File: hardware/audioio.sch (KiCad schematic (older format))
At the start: 7 parts

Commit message: Start placement of parts
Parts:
- C22, C23: footprint (none) -> footprints:SMD0805-CAP-M
- D7, D8: footprint (none) -> footprints:SOT23-M
- FB3, FB4, FB5: footprint (none) -> footprints:SMD0805-FERRITE-M
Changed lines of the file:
@@
 $Descr A4 11693 8268
 encoding utf-8
-Sheet 6 6
+Sheet 4 6
 Title "poppimASiina Audio IO protection"
 Date "2016-05-21"
@@
 AR Path="/5741BEDA/573ECF35" Ref="FB6"  Part="1"
 AR Path="/5741C4B9/573ECF35" Ref="FB9"  Part="1"
-F 0 "FB9" H 6950 3550 50  0000 C CNN
+F 0 "FB3" H 6950 3550 50  0000 C CNN
 F 1 "FILTER" H 7000 3450 50  0000 C CNN
-F 2 "" H 7100 3300 50  0000 C CNN
+F 2 "footprints:SMD0805-FERRITE-M" H 7100 3300 50  0001 C CNN
 F 3 "" H 7100 3300 50  0000 C CNN
 	1    7100 3300
@@
 AR Path="/5741BEDA/573EEC33" Ref="FB7"  Part="1"
 AR Path="/5741C4B9/573EEC33" Ref="FB10"  Part="1"
-F 0 "FB10" H 6950 3300 50  0000 C CNN
+F 0 "FB4" H 6950 3300 50  0000 C CNN
 F 1 "FILTER" H 7000 3400 50  0000 C CNN
-F 2 "" H 7100 3500 50  0000 C CNN
+F 2 "footprints:SMD0805-FERRITE-M" H 7100 3500 50  0001 C CNN
 F 3 "" H 7100 3500 50  0000 C CNN
 	1    7100 3500
@@
 AR Path="/5741BEDA/573F1279" Ref="C24"  Part="1"
 AR Path="/5741C4B9/573F1279" Ref="C26"  Part="1"
-F 0 "C26" H 6225 4000 50  0000 L CNN
+F 0 "C22" H 6225 4000 50  0000 L CNN
 F 1 "47p" H 6225 3800 50  0000 L CNN
-F 2 "" H 6238 3750 50  0000 C CNN
+F 2 "footprints:SMD0805-CAP-M" H 6238 3750 50  0001 C CNN
 F 3 "" H 6200 3900 50  0000 C CNN
 	1    6200 3900
@@
 AR Path="/5741BEDA/573F1460" Ref="C25"  Part="1"
 AR Path="/5741C4B9/573F1460" Ref="C27"  Part="1"
-F 0 "C27" H 6475 4000 50  0000 L CNN
+F 0 "C23" H 6475 4000 50  0000 L CNN
 F 1 "47p" H 6475 3800 50  0000 L CNN
-F 2 "" H 6488 3750 50  0000 C CNN
+F 2 "footprints:SMD0805-CAP-M" H 6488 3750 50  0001 C CNN
 F 3 "" H 6450 3900 50  0000 C CNN
 	1    6450 3900
@@
 $EndComp
 $Comp
-L GNDA #PWR45
+L GNDA #PWR045
 U 1 1 573F1A89
 P 6450 4200
-AR Path="/574185DC/573F1A89" Ref="#PWR45"  Part="1"
-AR Path="/5741BEDA/573F1A89" Ref="#PWR46"  Part="1"
-AR Path="/5741C4B9/573F1A89" Ref="#PWR47"  Part="1"
-F 0 "#PWR47" H 6450 3950 50  0001 C CNN
+AR Path="/574185DC/573F1A89" Ref="#PWR045"  Part="1"
+AR Path="/5741BEDA/573F1A89" Ref="#PWR046"  Part="1"
+AR Path="/5741C4B9/573F1A89" Ref="#PWR047"  Part="1"
+F 0 "#PWR045" H 6450 3950 50  0001 C CNN
 F 1 "GNDA" H 6450 4050 50  0000 C CNN
 F 2 "" H 6450 4200 50  0000 C CNN
@@
 AR Path="/5741BEDA/573F8794" Ref="D9"  Part="1"
 AR Path="/5741C4B9/573F8794" Ref="D11"  Part="1"
-F 0 "D11" H 5300 3150 50  0000 C CNN
+F 0 "D7" H 5300 3150 50  0000 C CNN
 F 1 "BAT54S" H 5300 3050 50  0000 C CNN
-F 2 "" H 5300 2950 50  0000 C CNN
+F 2 "footprints:SOT23-M" H 5300 2950 50  0001 C CNN
 F 3 "" H 5300 2950 50  0000 C CNN
 	1    5300 2950
@@
 AR Path="/5741BEDA/573F8863" Ref="D10"  Part="1"
 AR Path="/5741C4B9/573F8863" Ref="D12"  Part="1"
-F 0 "D12" H 5300 3950 50  0000 C CNN
+F 0 "D8" H 5300 3950 50  0000 C CNN
 F 1 "BAT54S" H 5300 3850 50  0000 C CNN
-F 2 "" H 5300 3750 50  0000 C CNN
+F 2 "footprints:SOT23-M" H 5300 3750 50  0001 C CNN
 F 3 "" H 5300 3750 50  0000 C CNN
 	1    5300 3750
@@
 AR Path="/5741BEDA/5741A7F2" Ref="FB8"  Part="1"
 AR Path="/5741C4B9/5741A7F2" Ref="FB11"  Part="1"
-F 0 "FB11" H 6950 4400 50  0000 C CNN
+F 0 "FB5" H 6950 4400 50  0000 C CNN
 F 1 "FILTER" H 7000 4300 50  0000 C CNN
-F 2 "" H 7100 4150 50  0000 C CNN
+F 2 "footprints:SMD0805-FERRITE-M" H 7100 4150 50  0001 C CNN
 F 3 "" H 7100 4150 50  0000 C CNN
 	1    7100 4150

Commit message: Add resistors from audio IO to gnd, fixes #10
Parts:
- added R? (x2): 1Meg5, symbol R
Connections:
- net GNDA: now also R?.2, R?.2
- net LEFT_DEVICE: now also R?.1
- net RIGHT_DEVICE: now also R?.1
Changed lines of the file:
@@
 $Descr A4 11693 8268
 encoding utf-8
-Sheet 4 6
+Sheet 6 6
 Title "poppimASiina Audio IO protection"
 Date "2016-05-21"
@@
 RF filtering
 Wire Wire Line
-	4350 3500 6750 3500
-Wire Wire Line
-	4350 3300 6750 3300
+	3200 3500 6750 3500
+Wire Wire Line
+	3200 3300 6750 3300
 Wire Wire Line
 	5300 3300 5300 3150
@@
 AR Path="/5741BEDA/573ECF35" Ref="FB6"  Part="1"
 AR Path="/5741C4B9/573ECF35" Ref="FB9"  Part="1"
-F 0 "FB3" H 6950 3550 50  0000 C CNN
+F 0 "FB9" H 6950 3550 50  0000 C CNN
 F 1 "FILTER" H 7000 3450 50  0000 C CNN
 F 2 "footprints:SMD0805-FERRITE-M" H 7100 3300 50  0001 C CNN
@@
 AR Path="/5741BEDA/573EEC33" Ref="FB7"  Part="1"
 AR Path="/5741C4B9/573EEC33" Ref="FB10"  Part="1"
-F 0 "FB4" H 6950 3300 50  0000 C CNN
+F 0 "FB10" H 6950 3300 50  0000 C CNN
 F 1 "FILTER" H 7000 3400 50  0000 C CNN
 F 2 "footprints:SMD0805-FERRITE-M" H 7100 3500 50  0001 C CNN
@@
 AR Path="/5741BEDA/573F1279" Ref="C24"  Part="1"
 AR Path="/5741C4B9/573F1279" Ref="C26"  Part="1"
-F 0 "C22" H 6225 4000 50  0000 L CNN
+F 0 "C26" H 6225 4000 50  0000 L CNN
 F 1 "47p" H 6225 3800 50  0000 L CNN
 F 2 "footprints:SMD0805-CAP-M" H 6238 3750 50  0001 C CNN
@@
 AR Path="/5741BEDA/573F1460" Ref="C25"  Part="1"
 AR Path="/5741C4B9/573F1460" Ref="C27"  Part="1"
-F 0 "C23" H 6475 4000 50  0000 L CNN
+F 0 "C27" H 6475 4000 50  0000 L CNN
 F 1 "47p" H 6475 3800 50  0000 L CNN
 F 2 "footprints:SMD0805-CAP-M" H 6488 3750 50  0001 C CNN
@@
 AR Path="/5741BEDA/573F1A89" Ref="#PWR046"  Part="1"
 AR Path="/5741C4B9/573F1A89" Ref="#PWR047"  Part="1"
-F 0 "#PWR045" H 6450 3950 50  0001 C CNN
+F 0 "#PWR047" H 6450 3950 50  0001 C CNN
 F 1 "GNDA" H 6450 4050 50  0000 C CNN
 F 2 "" H 6450 4200 50  0000 C CNN
@@
 AR Path="/5741BEDA/573F8794" Ref="D9"  Part="1"
 AR Path="/5741C4B9/573F8794" Ref="D11"  Part="1"
-F 0 "D7" H 5300 3150 50  0000 C CNN
+F 0 "D11" H 5300 3150 50  0000 C CNN
 F 1 "BAT54S" H 5300 3050 50  0000 C CNN
 F 2 "footprints:SOT23-M" H 5300 2950 50  0001 C CNN
@@
 AR Path="/5741BEDA/573F8863" Ref="D10"  Part="1"
 AR Path="/5741C4B9/573F8863" Ref="D12"  Part="1"
-F 0 "D8" H 5300 3950 50  0000 C CNN
+F 0 "D12" H 5300 3950 50  0000 C CNN
 F 1 "BAT54S" H 5300 3850 50  0000 C CNN
 F 2 "footprints:SOT23-M" H 5300 3750 50  0001 C CNN
@@
 Text HLabel 7800 3400 2    60   BiDi ~ 0
 GROUND_CABLE
-Text HLabel 4350 3300 0    60   BiDi ~ 0
+Text HLabel 3200 3300 0    60   BiDi ~ 0
 LEFT_DEVICE
-Text HLabel 4350 3500 0    60   BiDi ~ 0
+Text HLabel 3200 3500 0    60   BiDi ~ 0
 RIGHT_DEVICE
 Text HLabel 4900 3750 0    60   Input ~ 0
@@
 AR Path="/5741BEDA/5741A7F2" Ref="FB8"  Part="1"
 AR Path="/5741C4B9/5741A7F2" Ref="FB11"  Part="1"
-F 0 "FB5" H 6950 4400 50  0000 C CNN
+F 0 "FB11" H 6950 4400 50  0000 C CNN
 F 1 "FILTER" H 7000 4300 50  0000 C CNN
 F 2 "footprints:SMD0805-FERRITE-M" H 7100 4150 50  0001 C CNN
@@
 Wire Wire Line
 	6200 4050 6200 4150
+$Comp
+L R R?
+U 1 1 57493FA0
+P 3500 3750
+F 0 "R?" V 3580 3750 50  0000 C CNN
+F 1 "1Meg5" V 3400 3750 50  0000 C CNN
+F 2 "" V 3430 3750 50  0000 C CNN
+F 3 "" H 3500 3750 50  0000 C CNN
+	1    3500 3750
+	1    0    0    -1
+$EndComp
+$Comp
+L R R?
+U 1 1 57493FED
+P 3750 3750
+F 0 "R?" V 3830 3750 50  0000 C CNN
+F 1 "1Meg5" V 3650 3750 50  0000 C CNN
+F 2 "" V 3680 3750 50  0000 C CNN
+F 3 "" H 3750 3750 50  0000 C CNN
+	1    3750 3750
+	1    0    0    -1
+$EndComp
+Wire Wire Line
+	3750 3600 3750 3300
+Connection ~ 3750 3300
+Wire Wire Line
+	3500 3600 3500 3500
+Connection ~ 3500 3500
+$Comp
+L GNDA #PWR?
+U 1 1 57494606
+P 3750 4150
+F 0 "#PWR?" H 3750 3900 50  0001 C CNN
+F 1 "GNDA" H 3750 4000 50  0000 C CNN
+F 2 "" H 3750 4150 50  0000 C CNN
+F 3 "" H 3750 4150 50  0000 C CNN
+	1    3750 4150
+	1    0    0    -1
+$EndComp
+Wire Wire Line
+	3750 3900 3750 4150
+Wire Wire Line
+	3500 3900 3500 4000
+Wire Wire Line
+	3500 4000 3750 4000
+Connection ~ 3750 4000
 $EndSCHEMATC

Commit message: Fix #8
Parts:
- gave numbers to parts that had none: 2
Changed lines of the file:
@@
 $EndComp
 $Comp
-L GNDA #PWR045
+L GNDA #PWR047
 U 1 1 573F1A89
 P 6450 4200
-AR Path="/574185DC/573F1A89" Ref="#PWR045"  Part="1"
-AR Path="/5741BEDA/573F1A89" Ref="#PWR046"  Part="1"
-AR Path="/5741C4B9/573F1A89" Ref="#PWR047"  Part="1"
-F 0 "#PWR047" H 6450 3950 50  0001 C CNN
+AR Path="/574185DC/573F1A89" Ref="#PWR047"  Part="1"
+AR Path="/5741BEDA/573F1A89" Ref="#PWR049"  Part="1"
+AR Path="/5741C4B9/573F1A89" Ref="#PWR051"  Part="1"
+F 0 "#PWR051" H 6450 3950 50  0001 C CNN
 F 1 "GNDA" H 6450 4050 50  0000 C CNN
 F 2 "" H 6450 4200 50  0000 C CNN
@@
 	6200 4050 6200 4150
 $Comp
-L R R?
+L R R601
 U 1 1 57493FA0
 P 3500 3750
-F 0 "R?" V 3580 3750 50  0000 C CNN
+AR Path="/5741C4B9/57493FA0" Ref="R601"  Part="1"
+AR Path="/574185DC/57493FA0" Ref="R401"  Part="1"
+AR Path="/5741BEDA/57493FA0" Ref="R501"  Part="1"
+F 0 "R601" V 3580 3750 50  0000 C CNN
 F 1 "1Meg5" V 3400 3750 50  0000 C CNN
 F 2 "" V 3430 3750 50  0000 C CNN
@@
 $EndComp
 $Comp
-L R R?
+L R R602
 U 1 1 57493FED
 P 3750 3750
-F 0 "R?" V 3830 3750 50  0000 C CNN
+AR Path="/5741C4B9/57493FED" Ref="R602"  Part="1"
+AR Path="/574185DC/57493FED" Ref="R402"  Part="1"
+AR Path="/5741BEDA/57493FED" Ref="R502"  Part="1"
+F 0 "R602" V 3830 3750 50  0000 C CNN
 F 1 "1Meg5" V 3650 3750 50  0000 C CNN
 F 2 "" V 3680 3750 50  0000 C CNN
@@
 Connection ~ 3500 3500
 $Comp
-L GNDA #PWR?
+L GNDA #PWR052
 U 1 1 57494606
 P 3750 4150
-F 0 "#PWR?" H 3750 3900 50  0001 C CNN
+AR Path="/5741C4B9/57494606" Ref="#PWR052"  Part="1"
+AR Path="/574185DC/57494606" Ref="#PWR048"  Part="1"
+AR Path="/5741BEDA/57494606" Ref="#PWR050"  Part="1"
+F 0 "#PWR052" H 3750 3900 50  0001 C CNN
 F 1 "GNDA" H 3750 4000 50  0000 C CNN
 F 2 "" H 3750 4150 50  0000 C CNN

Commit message: Update schematics
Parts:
- R29: renamed from R601; footprint (none) -> footprints:SMD0805-RES-M
- R30: renamed from R602; footprint (none) -> footprints:SMD0805-RES-M
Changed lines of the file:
@@
 $EndComp
 $Comp
-L GNDA #PWR048
+L GNDA #PWR51
 U 1 1 573F1A89
 P 6450 4200
-AR Path="/574185DC/573F1A89" Ref="#PWR048"  Part="1"
-AR Path="/5741BEDA/573F1A89" Ref="#PWR050"  Part="1"
-AR Path="/5741C4B9/573F1A89" Ref="#PWR052"  Part="1"
-F 0 "#PWR052" H 6450 3950 50  0001 C CNN
+AR Path="/574185DC/573F1A89" Ref="#PWR51"  Part="1"
+AR Path="/5741BEDA/573F1A89" Ref="#PWR53"  Part="1"
+AR Path="/5741C4B9/573F1A89" Ref="#PWR55"  Part="1"
+F 0 "#PWR55" H 6450 3950 50  0001 C CNN
 F 1 "GNDA" H 6450 4050 50  0000 C CNN
 F 2 "" H 6450 4200 50  0000 C CNN
@@
 	6200 4050 6200 4150
 $Comp
-L R R601
+L R R29
 U 1 1 57493FA0
 P 3500 3750
-AR Path="/5741C4B9/57493FA0" Ref="R601"  Part="1"
-AR Path="/574185DC/57493FA0" Ref="R401"  Part="1"
-AR Path="/5741BEDA/57493FA0" Ref="R501"  Part="1"
-F 0 "R601" V 3580 3750 50  0000 C CNN
+AR Path="/5741C4B9/57493FA0" Ref="R29"  Part="1"
+AR Path="/574185DC/57493FA0" Ref="R25"  Part="1"
+AR Path="/5741BEDA/57493FA0" Ref="R27"  Part="1"
+F 0 "R29" V 3580 3750 50  0000 C CNN
 F 1 "1Meg5" V 3400 3750 50  0000 C CNN
-F 2 "" V 3430 3750 50  0000 C CNN
+F 2 "footprints:SMD0805-RES-M" V 3430 3750 50  0001 C CNN
 F 3 "" H 3500 3750 50  0000 C CNN
 	1    3500 3750
@@
 $EndComp
 $Comp
-L R R602
+L R R30
 U 1 1 57493FED
 P 3750 3750
-AR Path="/5741C4B9/57493FED" Ref="R602"  Part="1"
-AR Path="/574185DC/57493FED" Ref="R402"  Part="1"
-AR Path="/5741BEDA/57493FED" Ref="R502"  Part="1"
-F 0 "R602" V 3830 3750 50  0000 C CNN
+AR Path="/5741C4B9/57493FED" Ref="R30"  Part="1"
+AR Path="/574185DC/57493FED" Ref="R26"  Part="1"
+AR Path="/5741BEDA/57493FED" Ref="R28"  Part="1"
+F 0 "R30" V 3830 3750 50  0000 C CNN
 F 1 "1Meg5" V 3650 3750 50  0000 C CNN
-F 2 "" V 3680 3750 50  0000 C CNN
+F 2 "footprints:SMD0805-RES-M" V 3680 3750 50  0001 C CNN
 F 3 "" H 3750 3750 50  0000 C CNN
 	1    3750 3750
@@
 Connection ~ 3500 3500
 $Comp
-L GNDA #PWR053
+L GNDA #PWR54
 U 1 1 57494606
 P 3750 4150
-AR Path="/5741C4B9/57494606" Ref="#PWR053"  Part="1"
-AR Path="/574185DC/57494606" Ref="#PWR049"  Part="1"
-AR Path="/5741BEDA/57494606" Ref="#PWR051"  Part="1"
-F 0 "#PWR053" H 3750 3900 50  0001 C CNN
+AR Path="/5741C4B9/57494606" Ref="#PWR54"  Part="1"
+AR Path="/574185DC/57494606" Ref="#PWR50"  Part="1"
+AR Path="/5741BEDA/57494606" Ref="#PWR52"  Part="1"
+F 0 "#PWR54" H 3750 3900 50  0001 C CNN
 F 1 "GNDA" H 3750 4000 50  0000 C CNN
 F 2 "" H 3750 4150 50  0000 C CNN

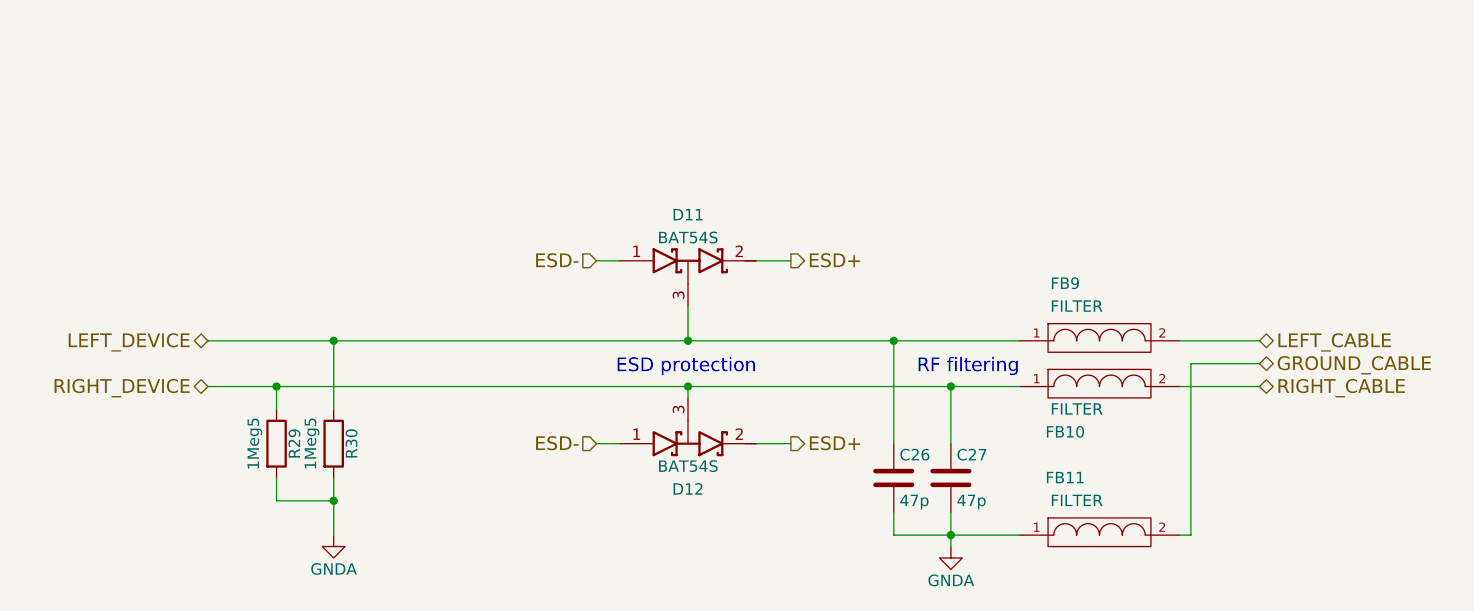
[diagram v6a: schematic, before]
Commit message: Make minimal circuitry
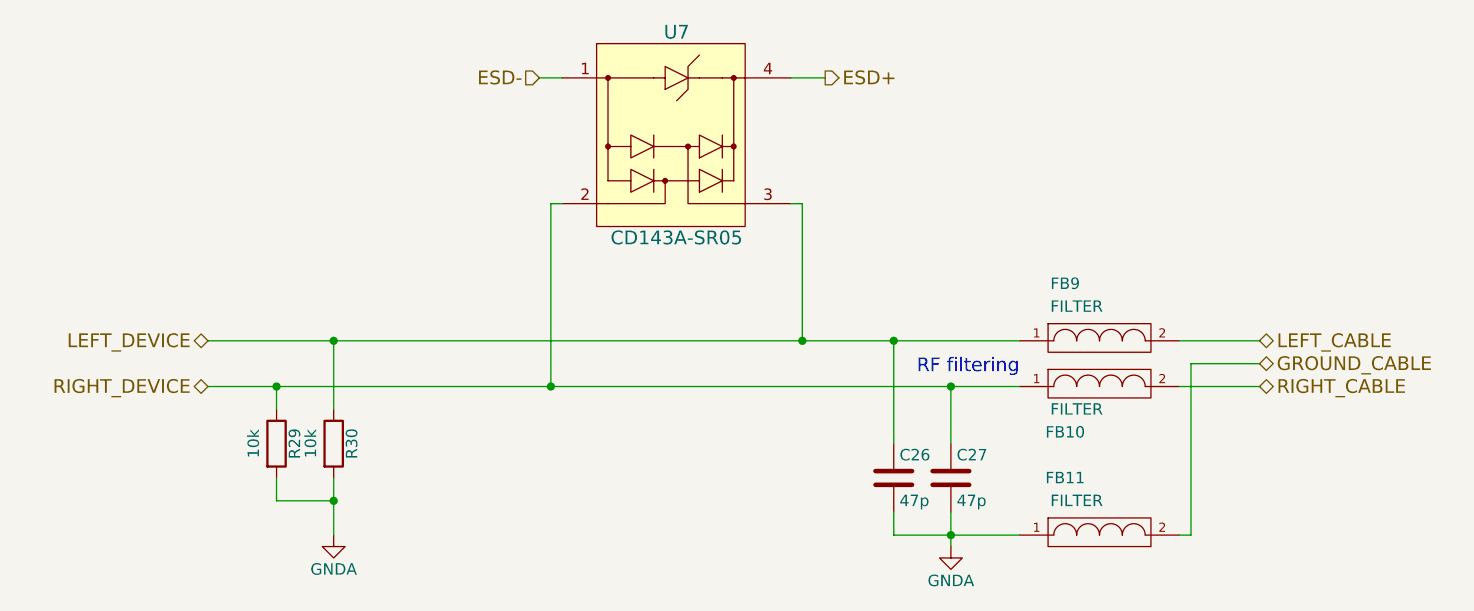
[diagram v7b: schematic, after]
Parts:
- removed D7, D8: BAT54S, footprints:SOT23-M, symbol BAT54S
- added U7: CD143A-SR05, footprints:SOT143-N, symbol CD143A-SR05
- C22, C23: footprint footprints:SMD0805-CAP-M -> footprints:SMD0402-CAP-N
- FB3, FB4, FB5: footprint footprints:SMD0805-FERRITE-M -> footprints:SMD0402-FERRITE-N
- R29, R30: value 1Meg5 -> 10k; footprint footprints:SMD0805-RES-M -> footprints:SMD0402-RES-N
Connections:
- net ESD+: now also U7.4
- net ESD-: now also U7.1
- net LEFT_DEVICE: now also U7.3
- net RIGHT_DEVICE: now also U7.2
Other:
- note removed: "ESD protection"
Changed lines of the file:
@@
 LIBS:bat54s
 LIBS:tps22860
+LIBS:cd143a-sr05
+LIBS:lm2776
+LIBS:linear
 LIBS:musamasiina-cache
 EELAYER 25 0
@@
 $Descr A4 11693 8268
 encoding utf-8
-Sheet 6 6
+Sheet 3 3
 Title "poppimASiina Audio IO protection"
 Date "2016-05-21"
@@
 Comment4 "ojousima / otso@ojousima.net"
 $EndDescr
-Text Notes 5600 3450 2    60   ~ 0
-ESD protection
 Text Notes 6750 3450 2    60   ~ 0
 RF filtering
@@
 	3200 3300 6750 3300
 Wire Wire Line
-	5300 3300 5300 3150
-Connection ~ 5300 3300
-Wire Wire Line
-	4900 3750 5000 3750
-Wire Wire Line
-	4900 2950 5000 2950
+	4650 2150 4750 2150
 $Comp
 L FILTER FB3
@@
 F 0 "FB9" H 6950 3550 50  0000 C CNN
 F 1 "FILTER" H 7000 3450 50  0000 C CNN
-F 2 "footprints:SMD0805-FERRITE-M" H 7100 3300 50  0001 C CNN
+F 2 "footprints:SMD0402-FERRITE-N" H 7100 3300 50  0001 C CNN
 F 3 "" H 7100 3300 50  0000 C CNN
 	1    7100 3300
@@
 F 0 "FB10" H 6950 3300 50  0000 C CNN
 F 1 "FILTER" H 7000 3400 50  0000 C CNN
-F 2 "footprints:SMD0805-FERRITE-M" H 7100 3500 50  0001 C CNN
+F 2 "footprints:SMD0402-FERRITE-N" H 7100 3500 50  0001 C CNN
 F 3 "" H 7100 3500 50  0000 C CNN
 	1    7100 3500
 	1    0    0    -1
 $EndComp
-Wire Wire Line
-	5300 3550 5300 3500
-Connection ~ 5300 3500
 $Comp
 L C C22
@@
 F 0 "C26" H 6225 4000 50  0000 L CNN
 F 1 "47p" H 6225 3800 50  0000 L CNN
-F 2 "footprints:SMD0805-CAP-M" H 6238 3750 50  0001 C CNN
+F 2 "footprints:SMD0402-CAP-N" H 6238 3750 50  0001 C CNN
 F 3 "" H 6200 3900 50  0000 C CNN
 	1    6200 3900
@@
 F 0 "C27" H 6475 4000 50  0000 L CNN
 F 1 "47p" H 6475 3800 50  0000 L CNN
-F 2 "footprints:SMD0805-CAP-M" H 6488 3750 50  0001 C CNN
+F 2 "footprints:SMD0402-CAP-N" H 6488 3750 50  0001 C CNN
 F 3 "" H 6450 3900 50  0000 C CNN
 	1    6450 3900
@@
 $EndComp
 $Comp
-L GNDA #PWR51
+L GNDA #PWR051
 U 1 1 573F1A89
 P 6450 4200
-AR Path="/574185DC/573F1A89" Ref="#PWR51"  Part="1"
-AR Path="/5741BEDA/573F1A89" Ref="#PWR53"  Part="1"
-AR Path="/5741C4B9/573F1A89" Ref="#PWR55"  Part="1"
-F 0 "#PWR55" H 6450 3950 50  0001 C CNN
+AR Path="/574185DC/573F1A89" Ref="#PWR051"  Part="1"
+AR Path="/5741BEDA/573F1A89" Ref="#PWR053"  Part="1"
+AR Path="/5741C4B9/573F1A89" Ref="#PWR043"  Part="1"
+F 0 "#PWR043" H 6450 3950 50  0001 C CNN
 F 1 "GNDA" H 6450 4050 50  0000 C CNN
 F 2 "" H 6450 4200 50  0000 C CNN
@@
 Wire Wire Line
 	6450 4050 6450 4200
-$Comp
-L BAT54S D7
-U 1 1 573F8794
-P 5300 2950
-AR Path="/574185DC/573F8794" Ref="D7"  Part="1"
-AR Path="/5741BEDA/573F8794" Ref="D9"  Part="1"
-AR Path="/5741C4B9/573F8794" Ref="D11"  Part="1"
-F 0 "D11" H 5300 3150 50  0000 C CNN
-F 1 "BAT54S" H 5300 3050 50  0000 C CNN
-F 2 "footprints:SOT23-M" H 5300 2950 50  0001 C CNN
-F 3 "" H 5300 2950 50  0000 C CNN
-	1    5300 2950
-	1    0    0    -1
-$EndComp
-$Comp
-L BAT54S D8
-U 1 1 573F8863
-P 5300 3750
-AR Path="/574185DC/573F8863" Ref="D8"  Part="1"
-AR Path="/5741BEDA/573F8863" Ref="D10"  Part="1"
-AR Path="/5741C4B9/573F8863" Ref="D12"  Part="1"
-F 0 "D12" H 5300 3950 50  0000 C CNN
-F 1 "BAT54S" H 5300 3850 50  0000 C CNN
-F 2 "footprints:SOT23-M" H 5300 3750 50  0001 C CNN
-F 3 "" H 5300 3750 50  0000 C CNN
-	1    5300 3750
-	1    0    0    1
-$EndComp
 Wire Wire Line
 	7800 3300 7450 3300
@@
 Connection ~ 6200 3300
 Wire Wire Line
-	5600 2950 5750 2950
-Wire Wire Line
-	5600 3750 5750 3750
-Text HLabel 5750 2950 2    60   Output ~ 0
+	5750 2150 5900 2150
+Text HLabel 5900 2150 2    60   Output ~ 0
 ESD+
-Text HLabel 5750 3750 2    60   Output ~ 0
-ESD+
-Text HLabel 4900 2950 0    60   Input ~ 0
-ESD-
 Text HLabel 7800 3300 2    60   BiDi ~ 0
 LEFT_CABLE
@@
 Text HLabel 3200 3500 0    60   BiDi ~ 0
 RIGHT_DEVICE
-Text HLabel 4900 3750 0    60   Input ~ 0
-ESD-
 $Comp
 L FILTER FB5
@@
 F 0 "FB11" H 6950 4400 50  0000 C CNN
 F 1 "FILTER" H 7000 4300 50  0000 C CNN
-F 2 "footprints:SMD0805-FERRITE-M" H 7100 4150 50  0001 C CNN
+F 2 "footprints:SMD0402-FERRITE-N" H 7100 4150 50  0001 C CNN
 F 3 "" H 7100 4150 50  0000 C CNN
 	1    7100 4150
@@
 AR Path="/5741BEDA/57493FA0" Ref="R27"  Part="1"
 F 0 "R29" V 3580 3750 50  0000 C CNN
-F 1 "1Meg5" V 3400 3750 50  0000 C CNN
-F 2 "footprints:SMD0805-RES-M" V 3430 3750 50  0001 C CNN
+F 1 "10k" V 3400 3750 50  0000 C CNN
+F 2 "footprints:SMD0402-RES-N" V 3430 3750 50  0001 C CNN
 F 3 "" H 3500 3750 50  0000 C CNN
 	1    3500 3750
@@
 AR Path="/5741BEDA/57493FED" Ref="R28"  Part="1"
 F 0 "R30" V 3830 3750 50  0000 C CNN
-F 1 "1Meg5" V 3650 3750 50  0000 C CNN
-F 2 "footprints:SMD0805-RES-M" V 3680 3750 50  0001 C CNN
+F 1 "10k" V 3650 3750 50  0000 C CNN
+F 2 "footprints:SMD0402-RES-N" V 3680 3750 50  0001 C CNN
 F 3 "" H 3750 3750 50  0000 C CNN
 	1    3750 3750
@@
 Connection ~ 3500 3500
 $Comp
-L GNDA #PWR54
+L GNDA #PWR044
 U 1 1 57494606
 P 3750 4150
-AR Path="/5741C4B9/57494606" Ref="#PWR54"  Part="1"
-AR Path="/574185DC/57494606" Ref="#PWR50"  Part="1"
-AR Path="/5741BEDA/57494606" Ref="#PWR52"  Part="1"
-F 0 "#PWR54" H 3750 3900 50  0001 C CNN
+AR Path="/5741C4B9/57494606" Ref="#PWR044"  Part="1"
+AR Path="/574185DC/57494606" Ref="#PWR052"  Part="1"
+AR Path="/5741BEDA/57494606" Ref="#PWR054"  Part="1"
+F 0 "#PWR044" H 3750 3900 50  0001 C CNN
 F 1 "GNDA" H 3750 4000 50  0000 C CNN
 F 2 "" H 3750 4150 50  0000 C CNN
@@
 	3500 4000 3750 4000
 Connection ~ 3750 4000
+Text HLabel 4650 2150 0    60   Input ~ 0
+ESD-
+$Comp
+L CD143A-SR05 U7
+U 1 1 5753D2C9
+P 5250 2400
+F 0 "U7" H 5250 2850 60  0000 C CNN
+F 1 "CD143A-SR05" H 5250 1950 60  0000 C CNN
+F 2 "footprints:SOT143-N" H 5250 2500 60  0001 C CNN
+F 3 "" H 5250 2500 60  0000 C CNN
+	1    5250 2400
+	1    0    0    -1
+$EndComp
+Wire Wire Line
+	5750 2700 5800 2700
+Wire Wire Line
+	5800 2700 5800 3300
+Connection ~ 5800 3300
+Wire Wire Line
+	4750 2700 4700 2700
+Wire Wire Line
+	4700 2700 4700 3500
+Connection ~ 4700 3500
 $EndSCHEMATC
